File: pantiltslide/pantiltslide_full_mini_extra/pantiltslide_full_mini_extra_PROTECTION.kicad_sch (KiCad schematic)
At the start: 75 parts, among them J1 Conn_01x22_Socket, J17 Motor_Slide, J18 Motor_Pan, J19 Motor_Tilt, J2 Conn_01x22_Socket, J20 TCA9548A_Mux, J21 AS5600_Pan, J22 AS5600_Tilt, J23 OLED, J24 TCA9548A_Mux, J26 Limit_Min, J27 Limit_Max, J28 Motor_Aux, J29 Enc_Slide, J3 MUX_2, J30 Enc_Pan, J31 Enc_Tilt, J32 Enc_Aux, J33 Btn_SetKeyframe, J34 Btn_ClearKeyframe, J35 Btn_PlayPause, J36 Btn_Reset, J37 5V_In, J38 24V_In, J4 MUX_3, J41 Aux_Max, J5 MUX_4, J6 MUX_5, J7 MUX_6, J8 MUX_7, U1 tmc2209, U2 tmc2209, U3 tmc2209, U4 tmc2209

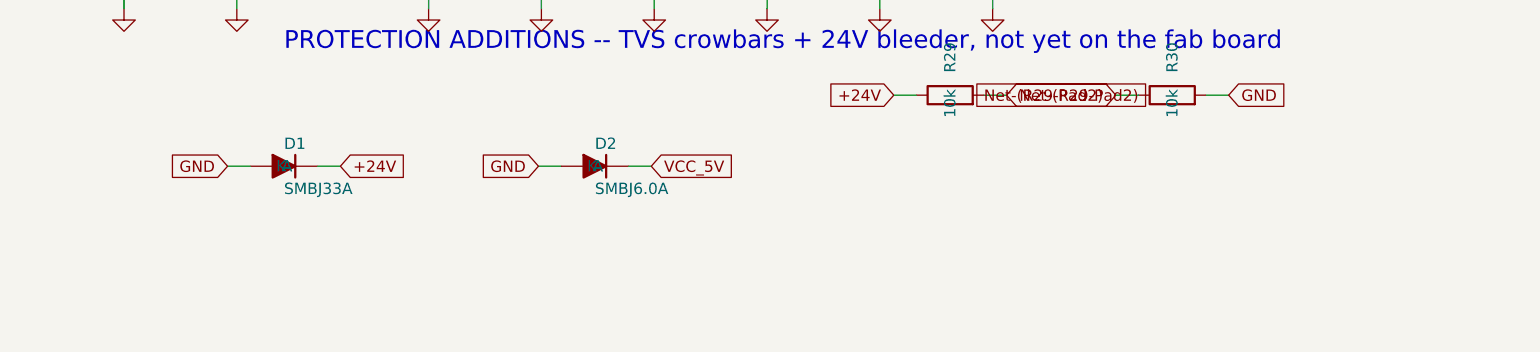
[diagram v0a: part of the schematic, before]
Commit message: Add power-indicator LEDs for 24V, 5V, 3.3V rails
LED1/R31 (24V), LED2/R32 (5V), LED3/R33 (3.3V) - one indicator per
supply rail, cathode to GND, anode through a series resistor to the
rail. R31 (10k) and R33 (1k) match the existing D4/R1 and D5/R2 design
in pantiltslide_full_pwr.kicad_sch exactly; R32 (2.2k) is new but reuses
an already-stocked resistor value from this same board (R5-R8).

Estimated currents at ~2.1V LED Vf: 24V/10k=2.2mA, 5V/2.2k=1.3mA,
3.3V/1k=1.2mA - all comfortably below any 0805 LED's rated max, though
not perfectly matched brightness across all three.

Device:LED symbol copied byte-for-byte from pantiltslide_full_pwr.kicad_sch
rather than hand-built, so it doesn't carry the cosmetic lib_symbol_mismatch
warning the earlier Device:D addition has.

Verified via netlist export (81 components, all 3 rails confirmed
correctly wired to their LED/resistor pair) and ERC (0 errors).

PCB placement not yet done.

Co-Authored-By: Claude Sonnet 5 <noreply@anthropic.com>
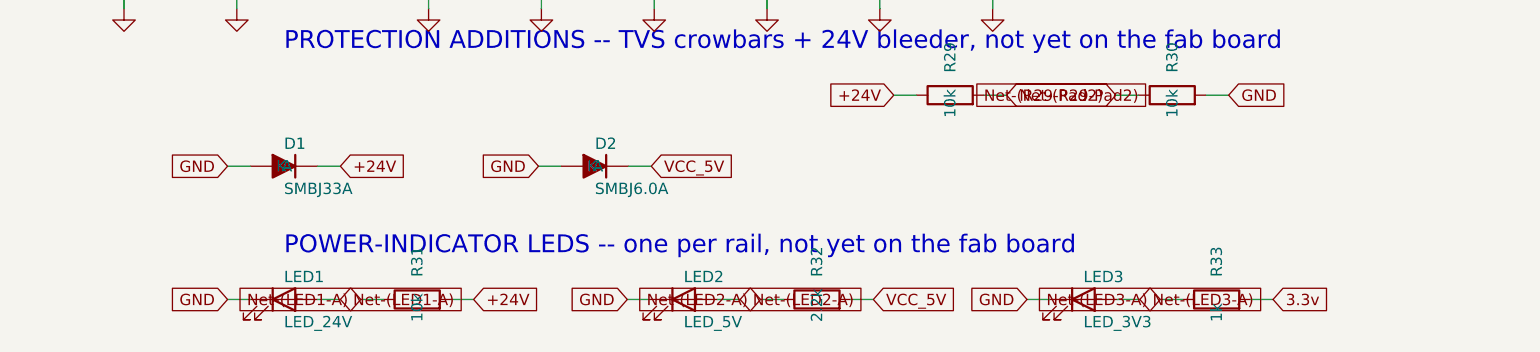
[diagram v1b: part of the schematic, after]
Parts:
- added LED1: LED_24V, LED_SMD:LED_0805_2012Metric, symbol Device:LED
- added LED2: LED_5V, LED_SMD:LED_0805_2012Metric, symbol Device:LED
- added LED3: LED_3V3, LED_SMD:LED_0805_2012Metric, symbol Device:LED
- added R31: 10k, Resistor_SMD:R_0805_2012Metric, symbol Device:R
- added R32: 2.2k, Resistor_SMD:R_0805_2012Metric, symbol Device:R
- added R33: 1k, Resistor_SMD:R_0805_2012Metric, symbol Device:R
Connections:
- net +24V: now also R31.2
- net +3.3V: now also R33.2
- net +5V: now also R32.2
- net GND: now also LED1.1 (K), LED2.1 (K), LED3.1 (K)
- new net Net-(LED1-A): LED1.2 (A), R31.1
- new net Net-(LED2-A): LED2.2 (A), R32.1
- new net Net-(LED3-A): LED3.2 (A), R33.1
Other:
- note added: "POWER-INDICATOR LEDS -- one per rail, not yet on the fab board"
